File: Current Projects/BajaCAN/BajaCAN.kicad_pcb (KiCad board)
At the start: 2 copper layers, 65.5 x 71.6 mm, 50 parts, among them J1 348300801, J2 348300804, J3 348302004, J4 348302001, U1 AVR128DB32x-xRXB, U2 MCP1603, U3 MCP251863T-H-SS, Y1 OV-7604-C7, Y2 CSTNE20M0V530000R0

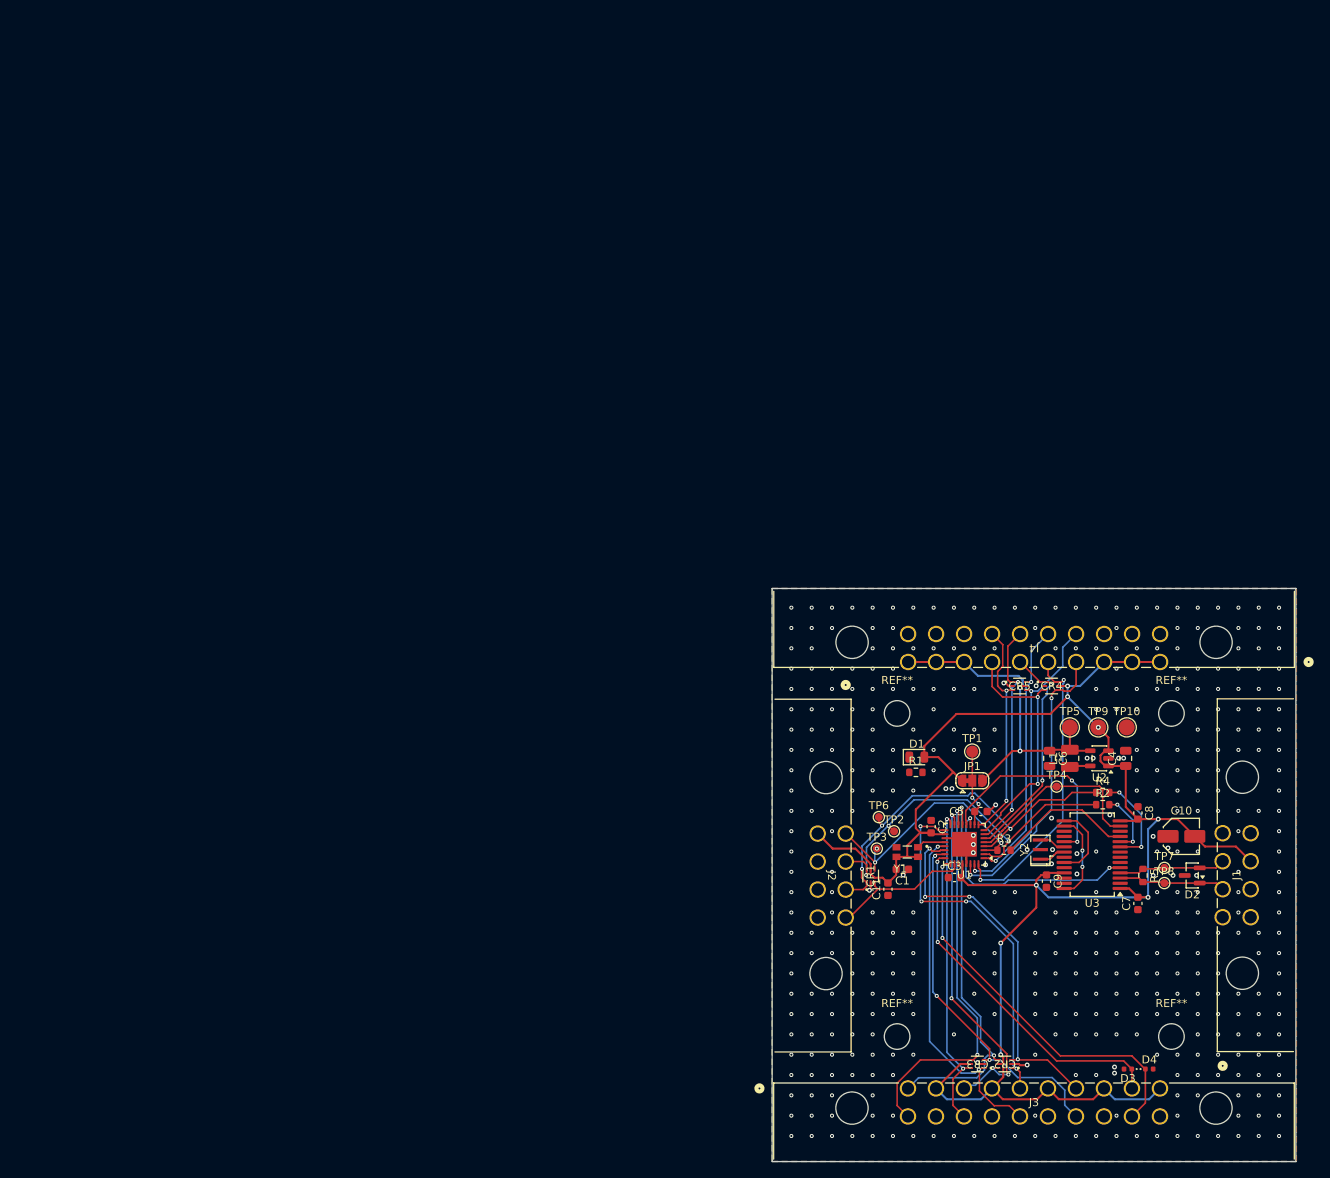
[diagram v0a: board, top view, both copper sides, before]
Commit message: Beginning footprint change on Baja CAN
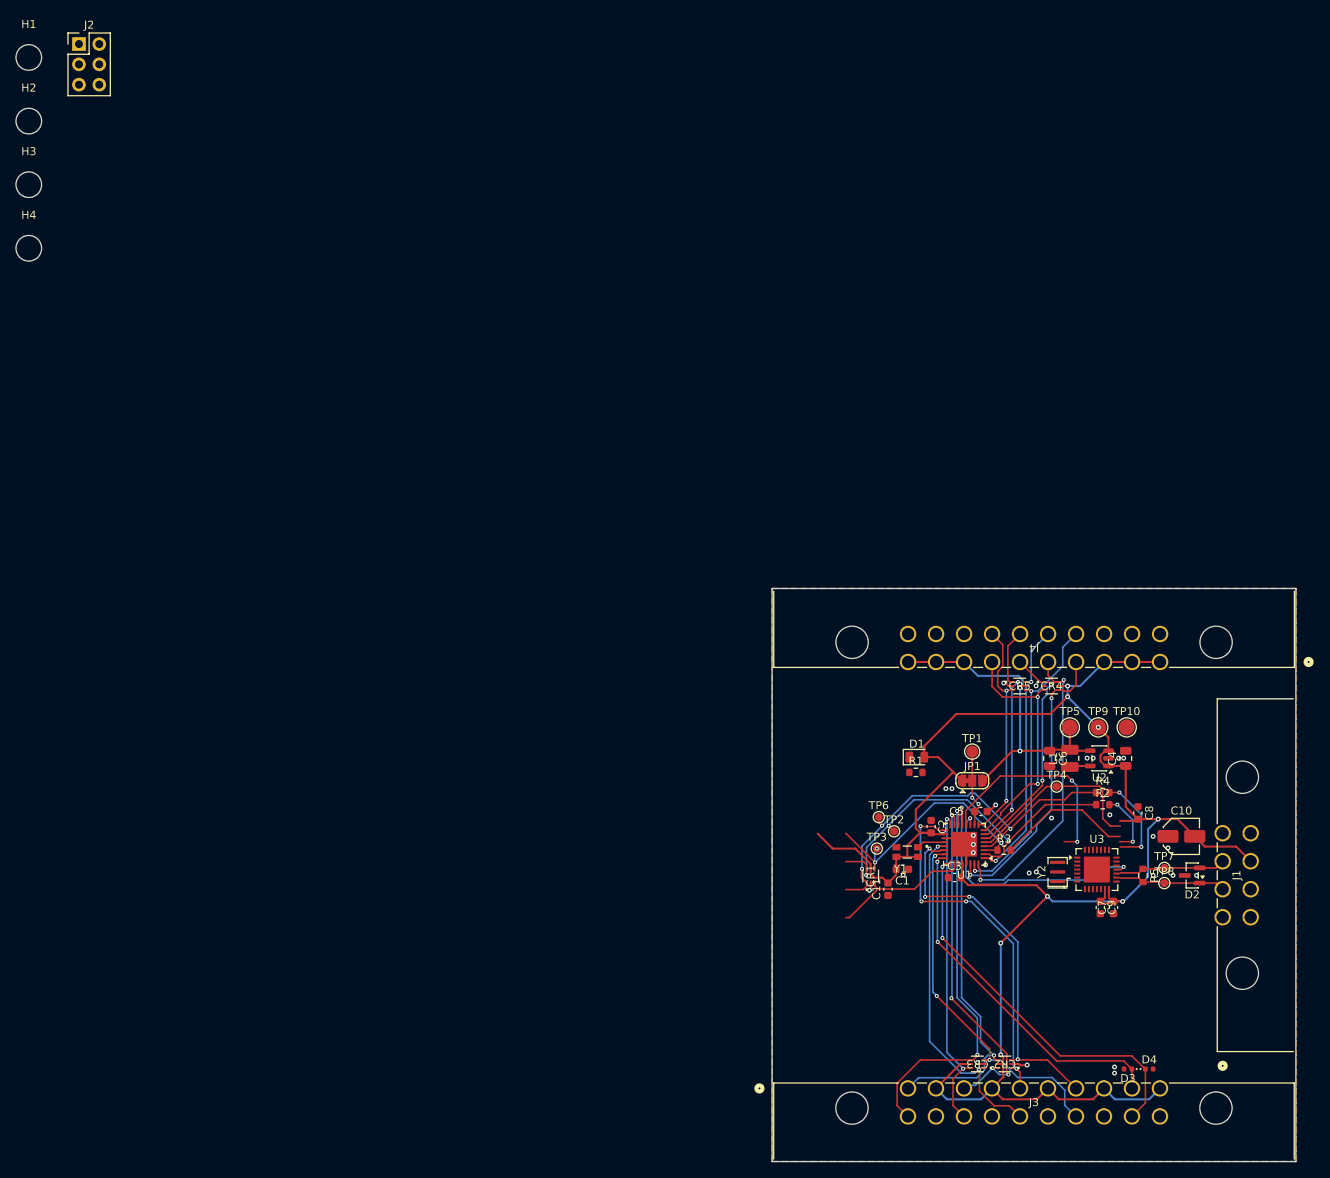
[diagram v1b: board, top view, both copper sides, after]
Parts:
- removed REF** (x4): MountingHole_3.2mm_M3, MountingHole:MountingHole_3.2mm_M3
- added H1: MountingHole, MountingHole:MountingHole_3.2mm_M3, F.Cu at (3.48, 3.48)
- added H2: MountingHole, MountingHole:MountingHole_3.2mm_M3, F.Cu at (3.48, 11.4)
- added H3: MountingHole, MountingHole:MountingHole_3.2mm_M3, F.Cu at (3.48, 19.4)
- added H4: MountingHole, MountingHole:MountingHole_3.2mm_M3, F.Cu at (3.48, 27.3)
- J2: value 348300804 -> ICSP; footprint molex:CONN_SD-34829-001_08_ST_MOL -> Connector_PinHeader_2.54mm:PinHeader_2x03_P2.54mm_Vertical
- U3: footprint Package_SO:SSOP-28_5.3x10.2mm_P0.65mm -> Package_DFN_QFN:VQFN-28-1EP_5x5mm_P0.5mm_EP3.25x3.25mm
- moved J2 137.6 mm to (9.74, 1.79), turned to 0 degrees
- moved C9 7.49 mm to (137.4, 109.7)
- moved Y2 3.53 mm to (132.1, 105.3)
- moved C7 3.09 mm to (139.1, 109.7)
- moved U3 1.95 mm to (137.0, 105.0), turned to 0 degrees
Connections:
- CR4 pad 1: MOSI1 -> SCK1
- CR4 pad 3: SCK1 -> ~{SS}1
- CR4 pad 4: TX0 -> MISO1
- CR4 pad 6: SDA0 -> MOSI1
- CR5 pad 1: MISO1 -> SDA0
- CR5 pad 3: ~{SS}1 -> SCL0
- CR5 pad 6: SCL0 -> TX0
- J2 pad 2: MOSI0 -> +5V
- J2 pad 4: ~{RESET} -> MOSI0
- J2 pad 5: +5V -> ~{RESET}
- J4 pad 15: SCL0 -> TX0
- J4 pad 16: MISO1 -> SDA0
- J4 pad 17: ~{SS}1 -> SCL0
- J4 pad 4: TX0 -> MISO1
- J4 pad 5: SDA0 -> MOSI1
- J4 pad 6: MOSI1 -> SCK1
- J4 pad 7: SCK1 -> ~{SS}1
- R2 pad 2: Net-(U3-SDI) -> /SDI
- R3 pad 2: Net-(U3-SDO) -> /SDO
- R4 pad 2: Net-(U3-SCK) -> /SCK
- U3 pad 1: +5V -> /RXD
- U3 pad 10: Net-(U3-SDI) -> GND
- U3 pad 11: Net-(U3-SDO) -> /RXD
- U3 pad 13: ~{SS}0 -> +5V
- U3 pad 15: Net-(U3-TXCAN) -> unconnected-(U3-NC-Pad15)
- U3 pad 16: Net-(U3-RXCAN) -> /CAN_L
- U3 pad 17: unconnected-(U3-NC-Pad17) -> /CAN_H
- U3 pad 18: unconnected-(U3-CLKO-Pad18) -> /MCP_STBY
- U3 pad 19: /MCP_INT -> unconnected-(U3-NC-Pad19)
- U3 pad 20: Net-(U3-OSC2) -> /TXD
- U3 pad 21: Net-(U3-OSC1) -> unconnected-(U3-NC-Pad21)
- U3 pad 22: GND -> /SCK
- U3 pad 23: Net-(U3-TXCAN) -> /SDI
- U3 pad 24: GND -> /SDO
- U3 pad 25: +5V -> ~{SS}0
- U3 pad 26: unconnected-(U3-NC-Pad26) -> +5V
- U3 pad 27: unconnected-(U3-NC-Pad27) -> (no net)
- U3 pad 28: Net-(U3-RXCAN) -> /TXD
- U3 pad 3: /CAN_L -> /MCP_INT
- U3 pad 4: /CAN_H -> /OSC1
- U3 pad 5: /MCP_STBY -> /OSC2
- U3 pad 7: unconnected-(U3-~{INT0}-Pad7) -> GND
- U3 pad 9: Net-(U3-SCK) -> unconnected-(U3-~{INT0}-Pad9)
- Y2 pad 1: Net-(U3-OSC1) -> /OSC2
- Y2 pad 3: Net-(U3-OSC2) -> /OSC1
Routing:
- net Net-(U3-SDO): track 17.2 -> 0.00 mm
- net /SDO: track 0.00 -> 17.2 mm
- net Net-(U3-SCK): track 11.9 -> 0.00 mm, vias 2 -> 0
- net /SCK: track 0.00 -> 11.9 mm, vias 0 -> 2
- net Net-(U3-RXCAN): track 11.1 -> 0.00 mm, vias 2 -> 0
- net Net-(U3-TXCAN): track 9.69 -> 0.00 mm
- net Net-(U3-SDI): track 8.01 -> 0.00 mm, vias 2 -> 0
- net /SDI: track 0.00 -> 8.01 mm, vias 0 -> 2
- net +5V: track 231.3 -> 227.7 mm
- net Net-(U3-OSC1): track 3.35 -> 0.00 mm
- net Net-(U3-OSC2): track 3.33 -> 0.00 mm
- net /MCP_STBY: track 28.9 -> 30.4 mm
- net GND: vias 428 -> 28

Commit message: Started CAN silkscreen
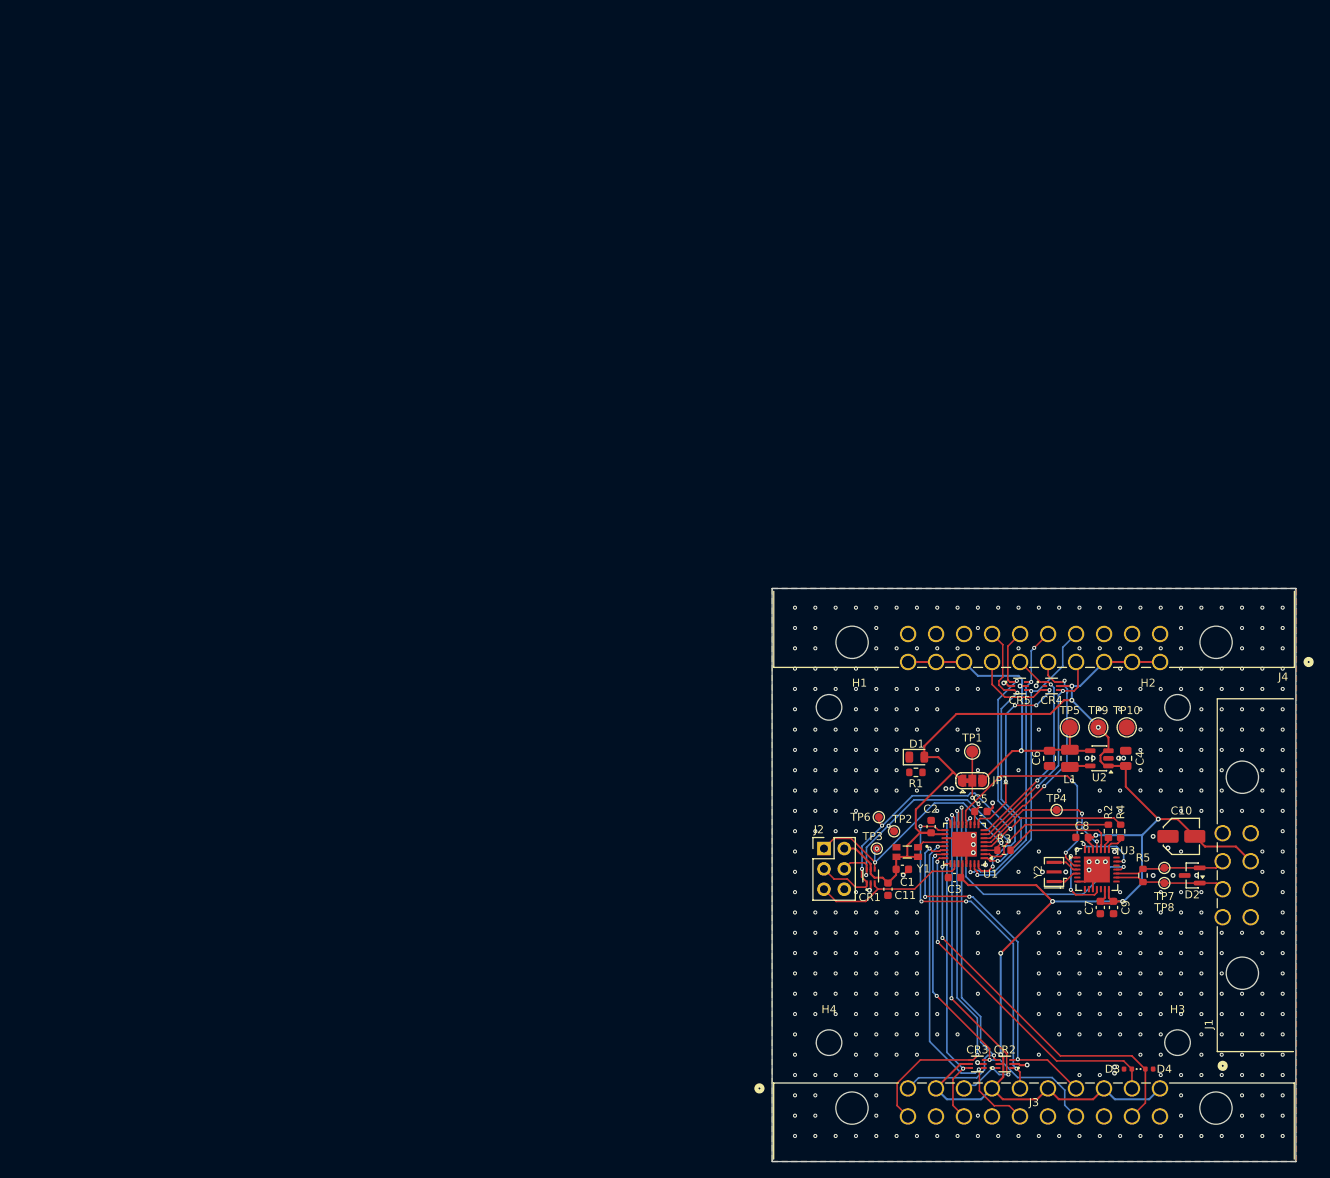
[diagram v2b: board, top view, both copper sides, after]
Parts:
- moved H3 179.2 mm to (147.1, 126.6)
- moved H2 161.2 mm to (147.1, 84.7)
- moved H4 140.9 mm to (103.5, 126.6)
- moved J2 137.1 mm to (102.9, 102.4)
- moved H1 128.9 mm to (103.5, 84.7)
- moved C8 7.63 mm to (135.1, 101.0), turned to 0 degrees
- moved R4 5.34 mm to (140.0, 100.2), turned to -90 degrees
- moved R2 3.40 mm to (138.4, 100.2), turned to -90 degrees
- moved TP4 2.92 mm to (132.0, 97.5)
- moved Y2 0.45 mm to (131.6, 105.3)
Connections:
- U3 pad 29: unconnected-(U3-NC-Pad29) -> GND
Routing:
- net /SCK: track 11.9 -> 2.57 mm, vias 2 -> 0
- net /RXD: track 0.00 -> 9.14 mm, vias 0 -> 2
- net /TXD: track 0.00 -> 8.17 mm, vias 0 -> 2
- net /SDI: track 8.01 -> 1.69 mm, vias 2 -> 0
- net GND: track 13.0 -> 18.8 mm, vias 28 -> 432
- net ~{SS}1: track 28.1 -> 33.8 mm, vias 2 -> 4
- net SCK0: track 49.3 -> 54.9 mm
- net ~{SS}0: track 24.1 -> 19.5 mm, vias 0 -> 2
- net SCK1: track 30.9 -> 27.3 mm
- net /OSC2: track 0.00 -> 3.32 mm
- net /OSC1: track 0.00 -> 3.28 mm
- net MISO0: track 31.7 -> 34.7 mm
- net /MCP_INT: track 26.7 -> 29.4 mm
- net SCL0: track 33.3 -> 36.0 mm
- net /SDO: track 17.2 -> 14.6 mm
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
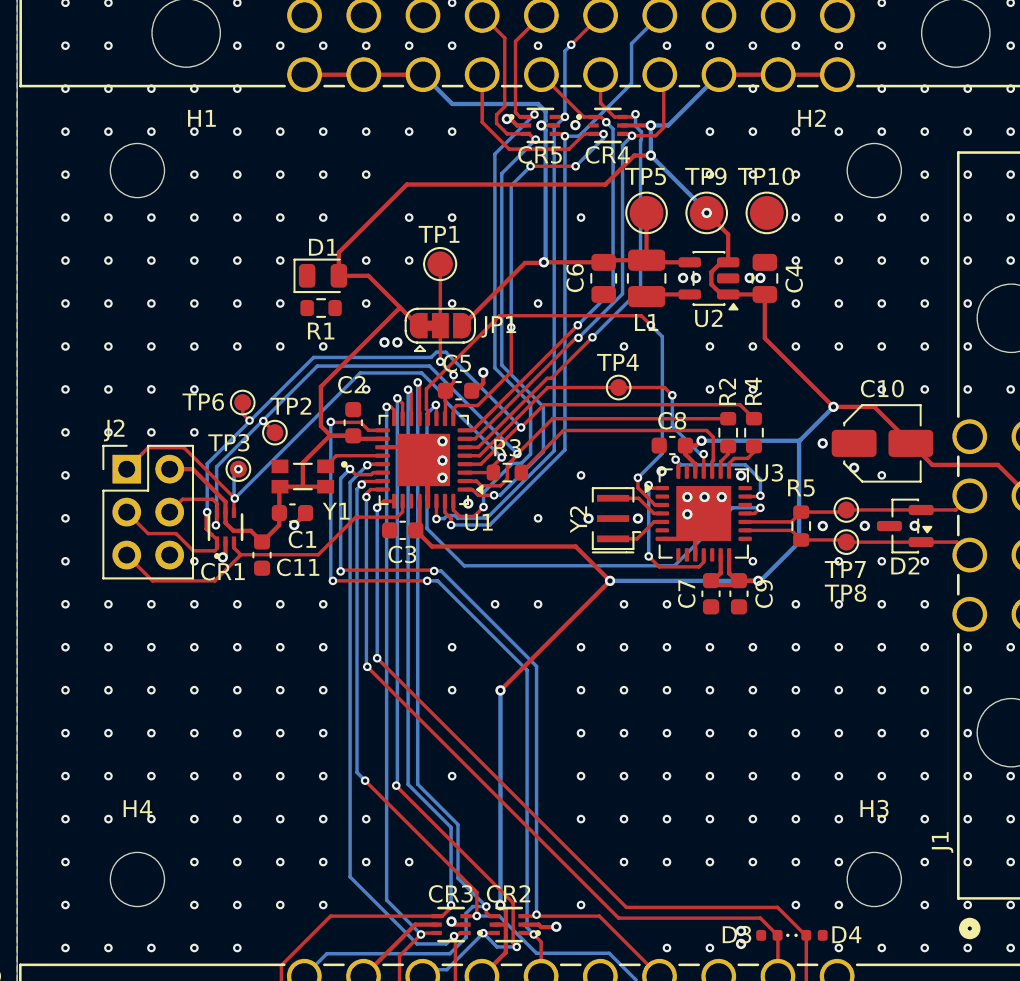
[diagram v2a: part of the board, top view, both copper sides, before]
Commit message: front silkscreen made
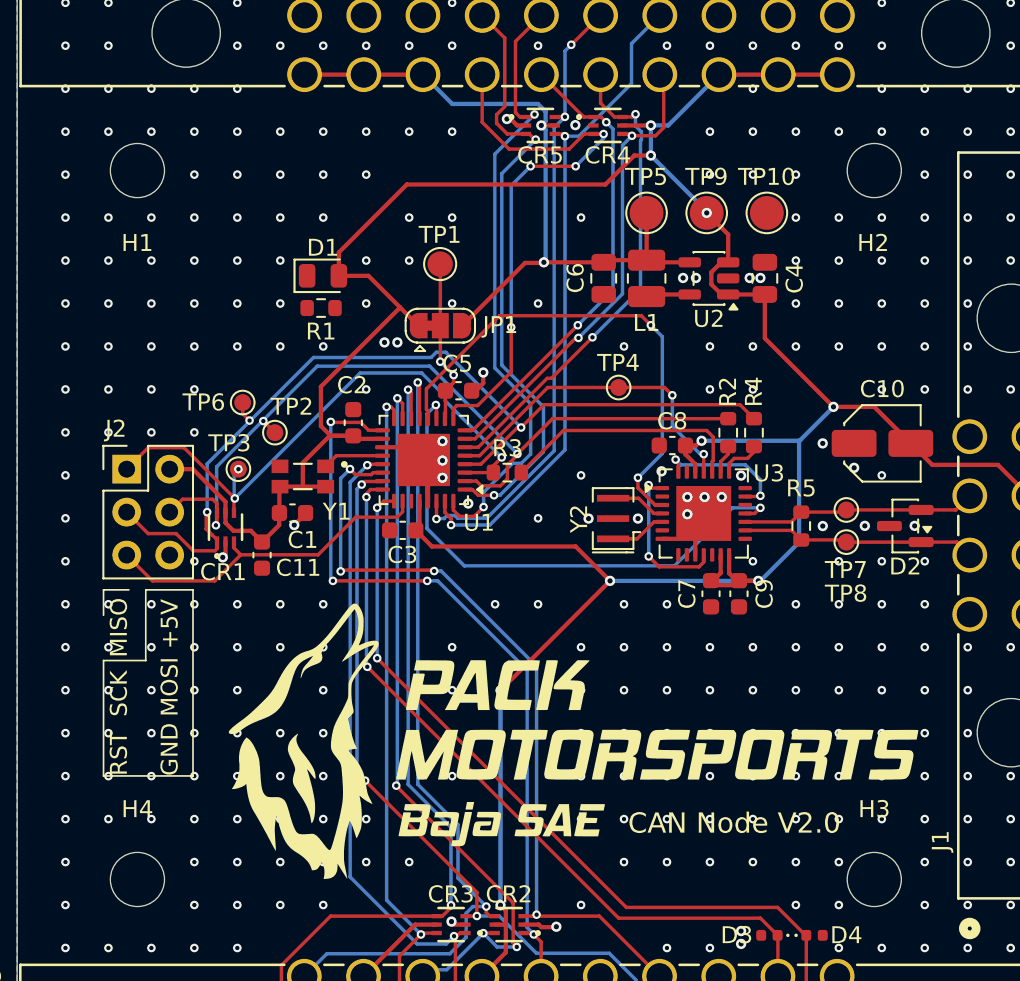
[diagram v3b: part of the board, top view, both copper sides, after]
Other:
- board text added: "+5V"
- board text added: "CAN Node V2.0"
- board text added: "GND"
- board text added: "MISO"
- board text added: "MOSI"
- board text added: "RST"
- board text added: "SCK"
